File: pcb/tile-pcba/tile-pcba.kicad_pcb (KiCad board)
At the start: 2 copper layers, 21.4 x 30.7 mm, 16 parts, among them IC1 THVD1420DR, J1 LED Strip, J2 UPDI, J5 12V, J6 RS-485 Jack, U1 ATtiny3224-X

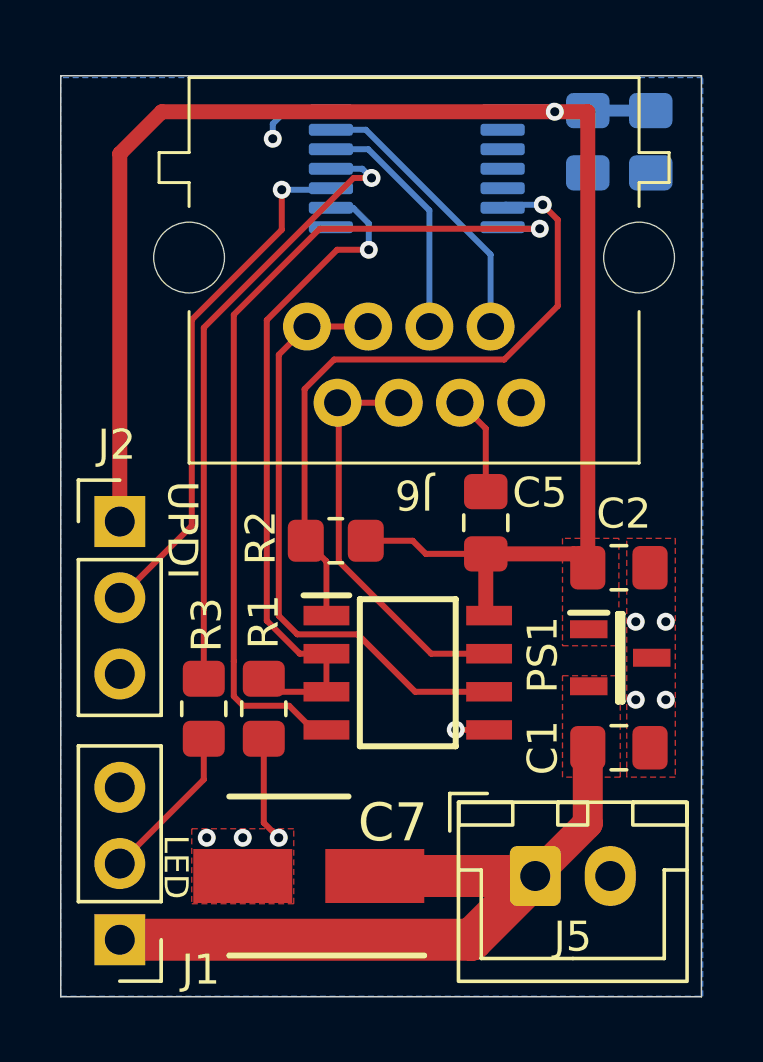
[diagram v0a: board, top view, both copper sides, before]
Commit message: Small changes the original tile, plus a pcba version with alternate parts that are available from JLCPCB.
Will likely collapse tile and tile-pcba once its confirmed tile-pcba is working
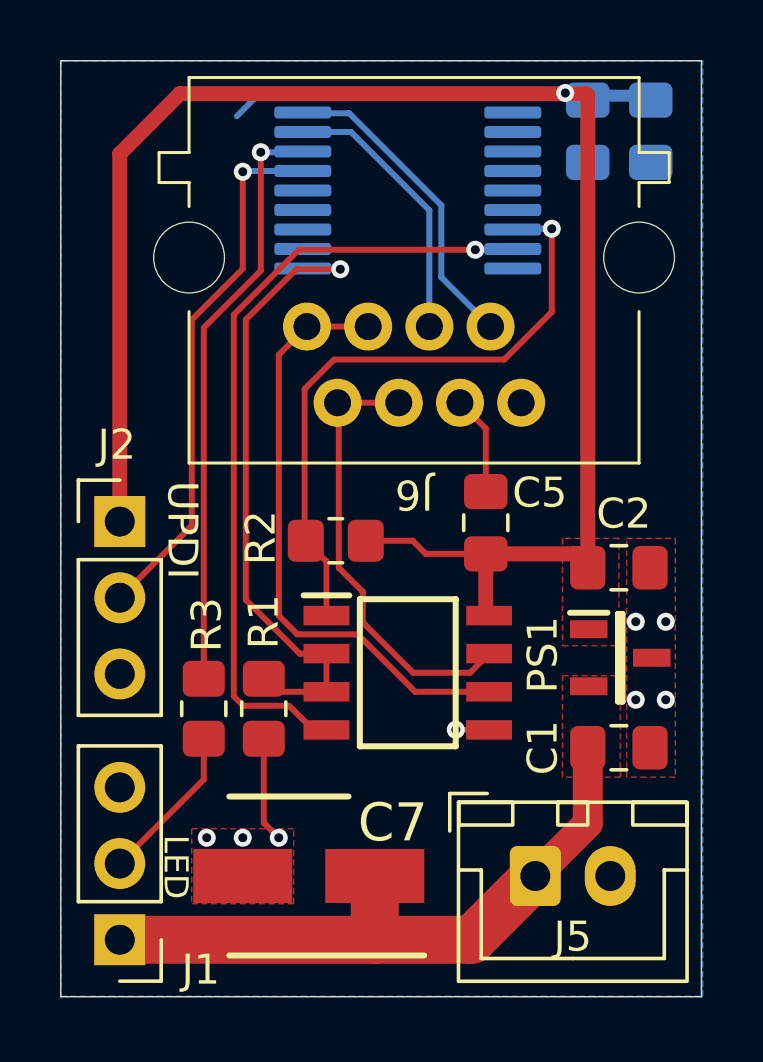
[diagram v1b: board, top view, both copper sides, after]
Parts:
- U1: value ATtiny3224-X -> ATtiny3226-X; footprint Package_SO:TSSOP-14_4.4x5mm_P0.65mm -> Package_SO:SSOP-20_5.3x7.2mm_P0.65mm
- moved U1 0.50 mm to (152.1, 68.2)
- moved C3 0.35 mm to (158.1, 66.5)
- moved C4 0.35 mm to (160.2, 66.5)
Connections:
- U1 pad 10: /UDPI_Data -> unconnected-(U1-PB1-Pad10)
- U1 pad 11: /LED_Data -> /XDIR
- U1 pad 12: /SENSE_IN -> unconnected-(U1-PC0-Pad12)
- U1 pad 13: /SENSE_OUT -> unconnected-(U1-PC1-Pad13)
- U1 pad 14: GND -> unconnected-(U1-PC2-Pad14)
- U1 pad 6: /RxD -> unconnected-(U1-PB5-Pad6)
- U1 pad 7: /TxD -> unconnected-(U1-PB4-Pad7)
- U1 pad 8: unconnected-(U1-PB1-Pad8) -> /RxD
- U1 pad 9: /XDIR -> /TxD
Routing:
- net +12V: track 25.1 -> 21.9 mm
- net /TxD: track 28.9 -> 26.5 mm
- net /XDIR: track 22.7 -> 21.4 mm
- net /TRCV-B: track 13.8 -> 15.1 mm
- net /SENSE_IN: track 8.00 -> 9.18 mm
- net /SENSE_OUT: track 9.45 -> 10.6 mm
- net /RxD: track 22.4 -> 21.2 mm
- net /LED_Data: track 20.8 -> 19.7 mm
- net +5V: track 59.4 -> 60.0 mm
- net GND: track 10.6 -> 10.5 mm, vias 9 -> 8
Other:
- board size 21.4 x 30.7 mm -> 21.4 x 31.2 mm
- board text added: "v1.3 2026-08-21"
- board text removed: "v1.2 2026-06-18"
